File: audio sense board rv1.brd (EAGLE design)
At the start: 130.8 x 26.7 mm, 33 parts, among them IC2 TSOP38238, J1 PJRAN1X1U01X, J2 PJRAN1X1U01X, Q1 2N3904, Q2 2N3904

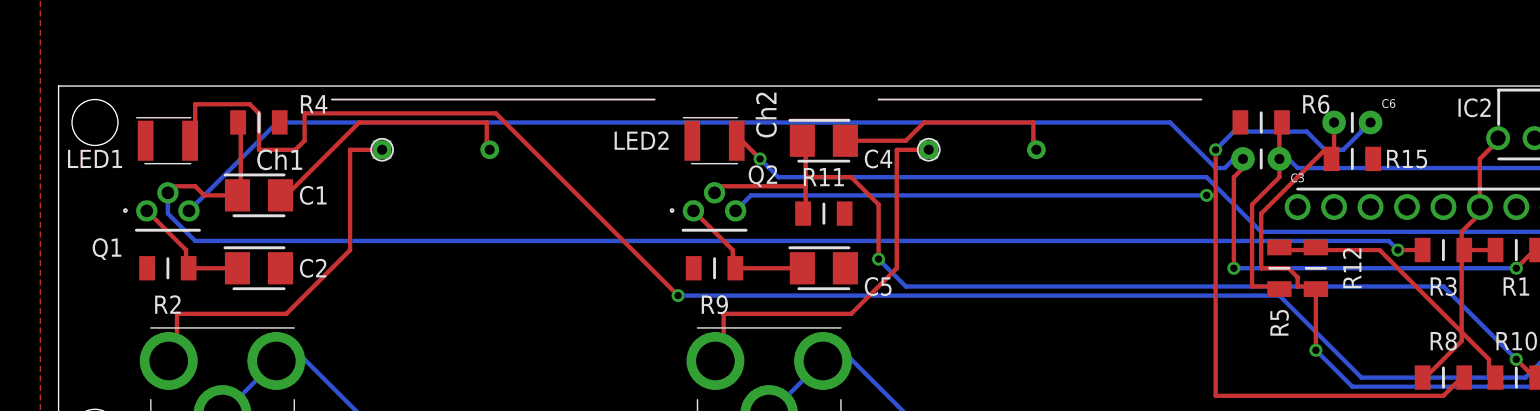
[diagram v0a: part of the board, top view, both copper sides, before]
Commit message: move labels
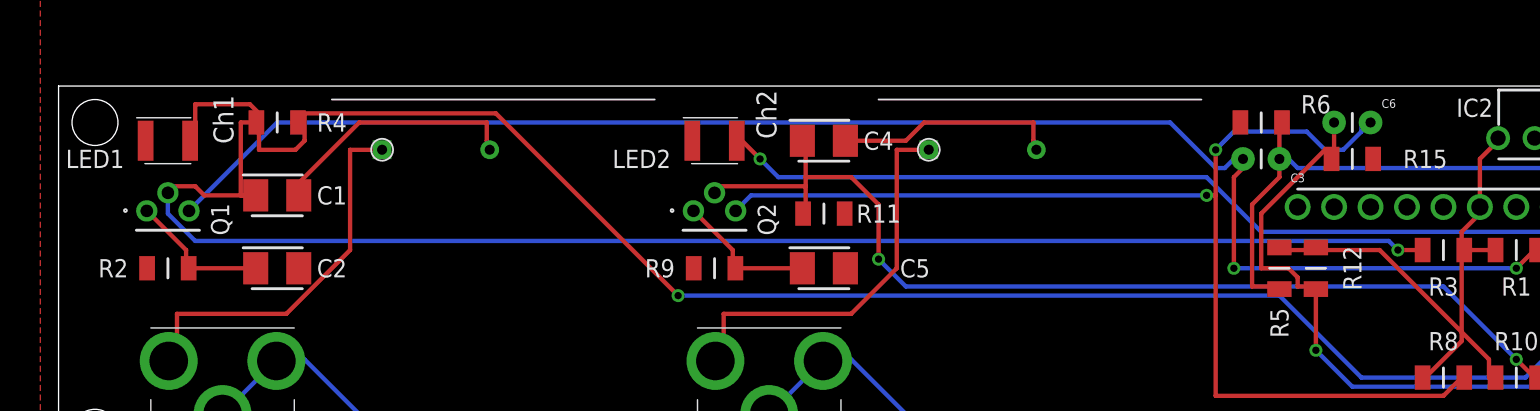
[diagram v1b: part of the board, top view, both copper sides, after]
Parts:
- moved C1 1.27 mm to (15.2, 17.8)
- moved C2 1.27 mm to (15.2, 12.7)
- moved R4 1.27 mm to (15.2, 22.9)
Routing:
- net N$16: track 101.0 -> 104.0 mm
- net N$20: track 8.72 -> 9.99 mm
- net N$17: track 18.4 -> 17.6 mm

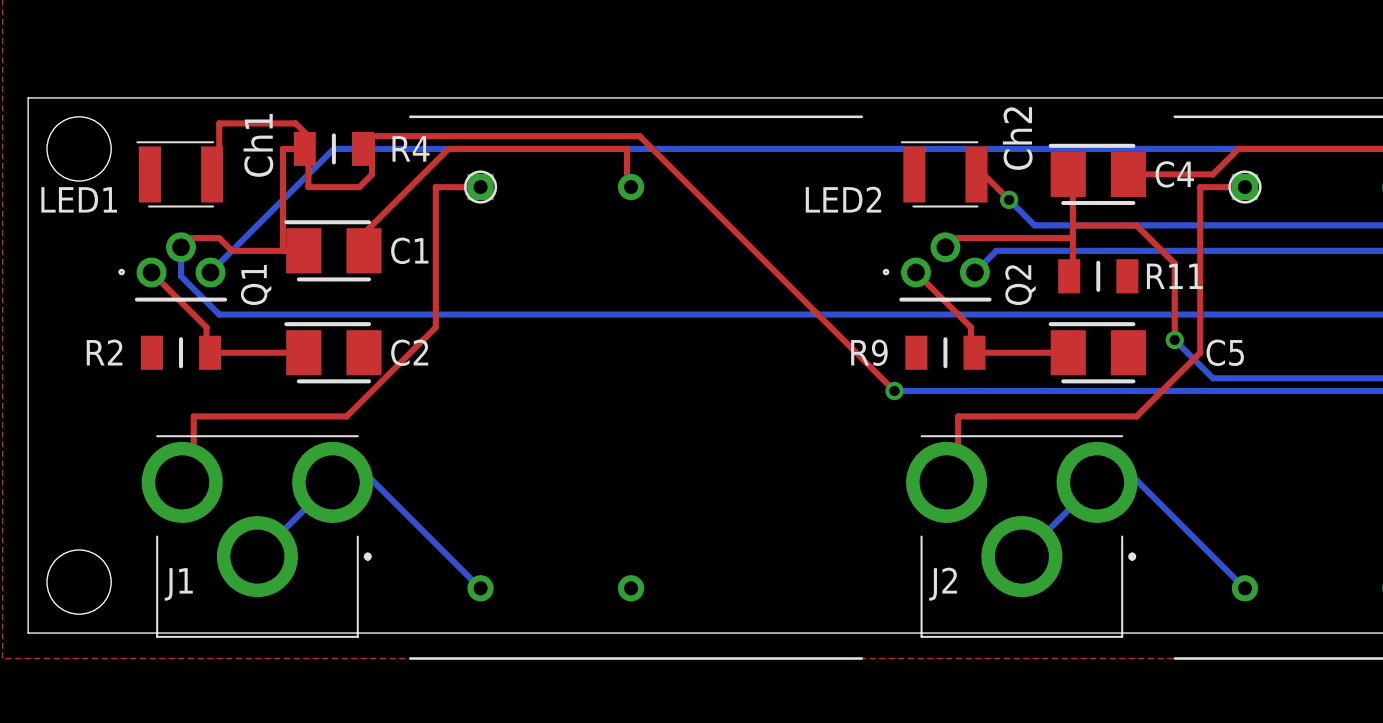
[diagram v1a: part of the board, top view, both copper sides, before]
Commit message: fix critical short on R4, overlaps and wire stubs
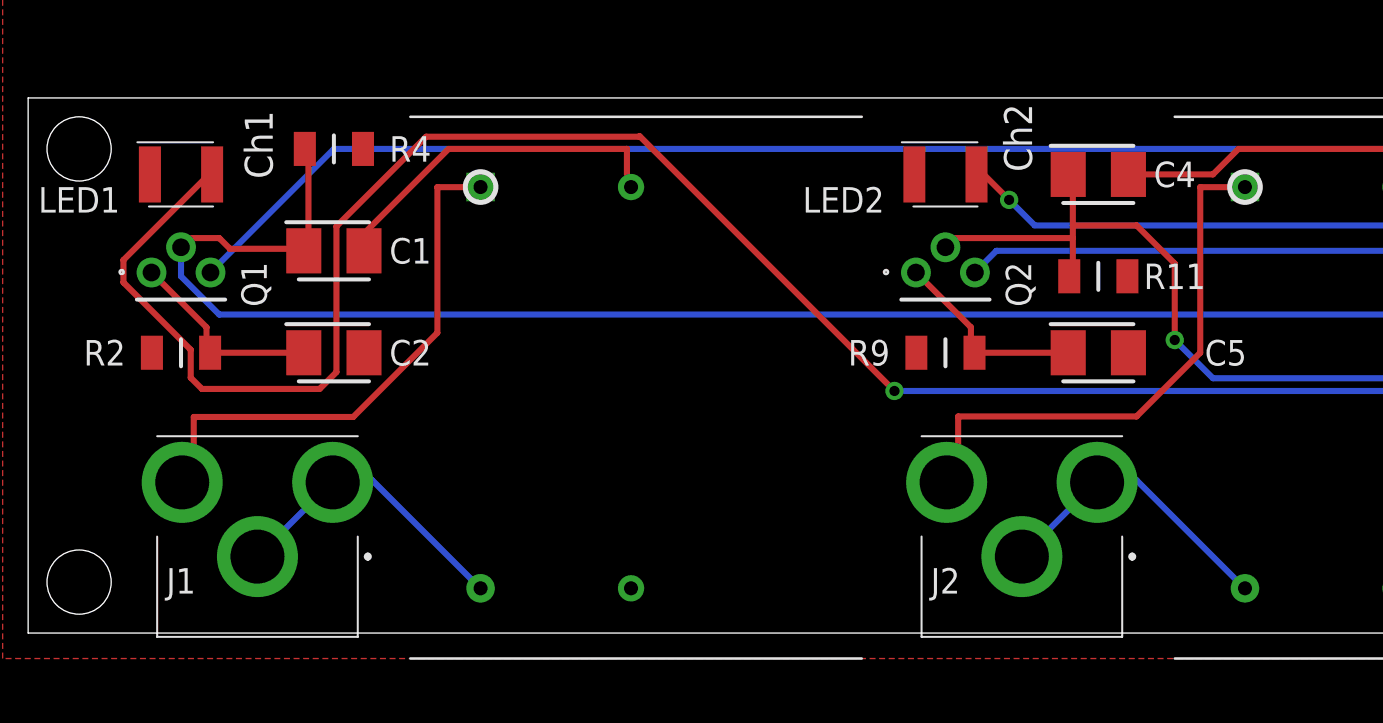
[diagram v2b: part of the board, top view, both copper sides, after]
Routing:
- net N$4: track 116.7 -> 133.4 mm
- net N$16: track 104.0 -> 102.1 mm
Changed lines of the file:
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@@
 <drawing>
 <settings>
-<setting alwaysvectorfont="yes"/>
+<setting alwaysvectorfont="no"/>
 <setting verticaltext="up"/>
 </settings>
 <grid distance="50" unitdist="mil" unit="mil" style="lines" multiple="1" display="yes" altdistance="5" altunitdist="mil" altunit="mil"/>
 <layers>
-<layer number="1" name="Top" color="4" fill="1" visible="no" active="yes"/>
+<layer number="1" name="Top" color="4" fill="1" visible="yes" active="yes"/>
 <layer number="16" name="Bottom" color="1" fill="1" visible="no" active="yes"/>
 <layer number="17" name="Pads" color="2" fill="1" visible="yes" active="yes"/>
@@
 <layer number="43" name="vRestrict" color="2" fill="10" visible="no" active="yes"/>
 <layer number="44" name="Drills" color="7" fill="1" visible="no" active="yes"/>
-<layer number="45" name="Holes" color="7" fill="1" visible="yes" active="yes"/>
+<layer number="45" name="Holes" color="7" fill="1" visible="no" active="yes"/>
 <layer number="46" name="Milling" color="3" fill="1" visible="no" active="yes"/>
 <layer number="47" name="Measures" color="7" fill="1" visible="no" active="yes"/>
@@
 <layer number="110" name="fp0" color="7" fill="1" visible="no" active="yes"/>
 <layer number="111" name="LPC17xx" color="7" fill="1" visible="no" active="yes"/>
-<layer number="112" name="tSilk" color="7" fill="1" visible="yes" active="yes"/>
+<layer number="112" name="tSilk" color="7" fill="1" visible="no" active="yes"/>
 <layer number="113" name="IDFDebug" color="7" fill="1" visible="no" active="yes"/>
 <layer number="114" name="Badge_Outline" color="7" fill="1" visible="no" active="yes"/>
@@
 <layer number="116" name="Patch_BOT" color="9" fill="4" visible="no" active="yes"/>
 <layer number="118" name="Rect_Pads" color="7" fill="1" visible="no" active="yes"/>
-<layer number="121" name="_tsilk" color="7" fill="1" visible="yes" active="yes"/>
+<layer number="121" name="_tsilk" color="7" fill="1" visible="no" active="yes"/>
 <layer number="122" name="_bsilk" color="7" fill="1" visible="no" active="yes"/>
 <layer number="123" name="tTestmark" color="7" fill="1" visible="no" active="yes"/>
@@
 <wire x1="43.18" y1="10.795" x2="85.09" y2="10.795" width="0.3048" layer="16"/>
 <wire x1="30.48" y1="23.495" x2="43.18" y2="10.795" width="0.3048" layer="1"/>
-<wire x1="17.145" y1="23.495" x2="30.48" y2="23.495" width="0.3048" layer="1"/>
-<wire x1="17.145" y1="21.59" x2="17.145" y2="23.495" width="0.3048" layer="1"/>
-<wire x1="16.51" y1="20.955" x2="17.145" y2="21.59" width="0.3048" layer="1"/>
-<wire x1="13.97" y1="20.955" x2="16.51" y2="20.955" width="0.3048" layer="1"/>
-<wire x1="13.97" y1="23.495" x2="13.97" y2="20.955" width="0.3048" layer="1"/>
-<wire x1="13.335" y1="24.13" x2="13.97" y2="23.495" width="0.3048" layer="1"/>
-<wire x1="9.525" y1="24.13" x2="13.335" y2="24.13" width="0.3048" layer="1"/>
-<wire x1="9.525" y1="21.59" x2="9.525" y2="24.13" width="0.3048" layer="1"/>
 <wire x1="107.95" y1="10.795" x2="107.95" y2="11.25" width="0.3048" layer="1"/>
-<wire x1="9.525" y1="21.59" x2="9.17" y2="21.59" width="0.3048" layer="1"/>
 <via x="104.14" y="6.985" extent="1-16" drill="0.508"/>
 <via x="43.18" y="10.795" extent="1-16" drill="0.508"/>
+<wire x1="4.7498" y1="17.3228" x2="8.9408" y2="21.5138" width="0.3048" layer="1"/>
+<wire x1="4.7498" y1="16.2052" x2="4.7498" y2="17.3228" width="0.3048" layer="1"/>
+<wire x1="8.1026" y1="12.8524" x2="4.7498" y2="16.2052" width="0.3048" layer="1"/>
+<wire x1="8.1026" y1="11.4554" x2="8.1026" y2="12.8524" width="0.3048" layer="1"/>
+<wire x1="8.6614" y1="10.8966" x2="8.1026" y2="11.4554" width="0.3048" layer="1"/>
+<wire x1="14.5288" y1="10.8966" x2="8.6614" y2="10.8966" width="0.3048" layer="1"/>
+<wire x1="15.367" y1="11.7348" x2="14.5288" y2="10.8966" width="0.3048" layer="1"/>
+<wire x1="15.367" y1="18.9992" x2="15.367" y2="11.7348" width="0.3048" layer="1"/>
+<wire x1="19.8374" y1="23.4696" x2="15.367" y2="18.9992" width="0.3048" layer="1"/>
+<wire x1="30.4546" y1="23.4696" x2="19.8374" y2="23.4696" width="0.3048" layer="1"/>
+<wire x1="8.9408" y1="21.5138" x2="9.17" y2="21.59" width="0.3048" layer="1"/>
+<wire x1="30.4546" y1="23.4696" x2="30.48" y2="23.495" width="0.3048" layer="1"/>
 </signal>
 <signal name="STATUS_CH1">
@@
 <contactref element="J1" pad="2"/>
 <contactref element="L1" pad="1"/>
-<wire x1="20.32" y1="20.955" x2="22.225" y2="20.955" width="0.3048" layer="1"/>
-<wire x1="20.32" y1="13.97" x2="20.32" y2="20.955" width="0.3048" layer="1"/>
-<wire x1="15.875" y1="9.525" x2="20.32" y2="13.97" width="0.3048" layer="1"/>
-<wire x1="8.255" y1="9.525" x2="15.875" y2="9.525" width="0.3048" layer="1"/>
-<wire x1="8.255" y1="6.35" x2="8.255" y2="9.525" width="0.3048" layer="1"/>
+<wire x1="20.3962" y1="20.955" x2="22.225" y2="20.955" width="0.3048" layer="1"/>
+<wire x1="8.255" y1="6.35" x2="8.255" y2="9.4996" width="0.3048" layer="1"/>
 <wire x1="22.225" y1="20.955" x2="22.55" y2="20.96" width="0.3048" layer="1"/>
 <wire x1="8.255" y1="6.35" x2="7.68" y2="6.24" width="0.3048" layer="1"/>
+<wire x1="20.3962" y1="13.6906" x2="20.3962" y2="20.955" width="0.3048" layer="1"/>
+<wire x1="16.2052" y1="9.4996" x2="20.3962" y2="13.6906" width="0.3048" layer="1"/>
+<wire x1="8.255" y1="9.4996" x2="16.2052" y2="9.4996" width="0.3048" layer="1"/>
 </signal>
 <signal name="N$17">
@@
 <contactref element="R3" pad="1"/>
 <contactref element="R4" pad="1"/>
-<wire x1="12.7" y1="17.78" x2="12.7" y2="22.86" width="0.3048" layer="1"/>
-<wire x1="12.7" y1="22.86" x2="13.79" y2="22.86" width="0.3048" layer="1"/>
-<wire x1="12.7" y1="17.78" x2="13.74" y2="17.78" width="0.3048" layer="1"/>
 <wire x1="93.345" y1="13.97" x2="95.07" y2="13.97" width="0.3048" layer="1"/>
 <wire x1="92.71" y1="14.605" x2="93.345" y2="13.97" width="0.3048" layer="16"/>
@@
 <wire x1="7.62" y1="16.51" x2="9.525" y2="14.605" width="0.3048" layer="16"/>
 <wire x1="7.62" y1="17.958" x2="7.62" y2="16.51" width="0.3048" layer="16"/>
-<wire x1="10.16" y1="17.78" x2="13.74" y2="17.78" width="0.3048" layer="1"/>
-<wire x1="9.525" y1="18.415" x2="10.16" y2="17.78" width="0.3048" layer="1"/>
+<wire x1="9.525" y1="18.415" x2="10.0584" y2="17.8816" width="0.3048" layer="1"/>
 <wire x1="7.62" y1="18.415" x2="9.525" y2="18.415" width="0.3048" layer="1"/>
 <wire x1="7.62" y1="18.415" x2="7.62" y2="17.958" width="0.3048" layer="1"/>
 <via x="93.345" y="13.97" extent="1-16" drill="0.508"/>
+<wire x1="13.97" y1="17.8816" x2="13.97" y2="22.6314" width="0.3048" layer="1"/>
+<wire x1="13.97" y1="22.6314" x2="13.79" y2="22.86" width="0.3048" layer="1"/>
+<wire x1="13.97" y1="17.8816" x2="13.74" y2="17.78" width="0.3048" layer="1"/>
+<wire x1="10.0584" y1="17.8816" x2="13.6906" y2="17.8816" width="0.3048" layer="1"/>
+<wire x1="13.6906" y1="17.8816" x2="13.74" y2="17.78" width="0.3048" layer="1"/>
 </signal>
 <signal name="N$20">
